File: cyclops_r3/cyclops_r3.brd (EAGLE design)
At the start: 124.5 x 79.9 mm, 105 parts, among them Q1 BC817, Q2 IRF510, U1 MCP4921, U2 MCP4022-50k, U3 317-N, U4 TLV3701, U5 337-N, U6 ADR03, U7 OP1177, U8 LTC2052HV, U9 ZXTD45

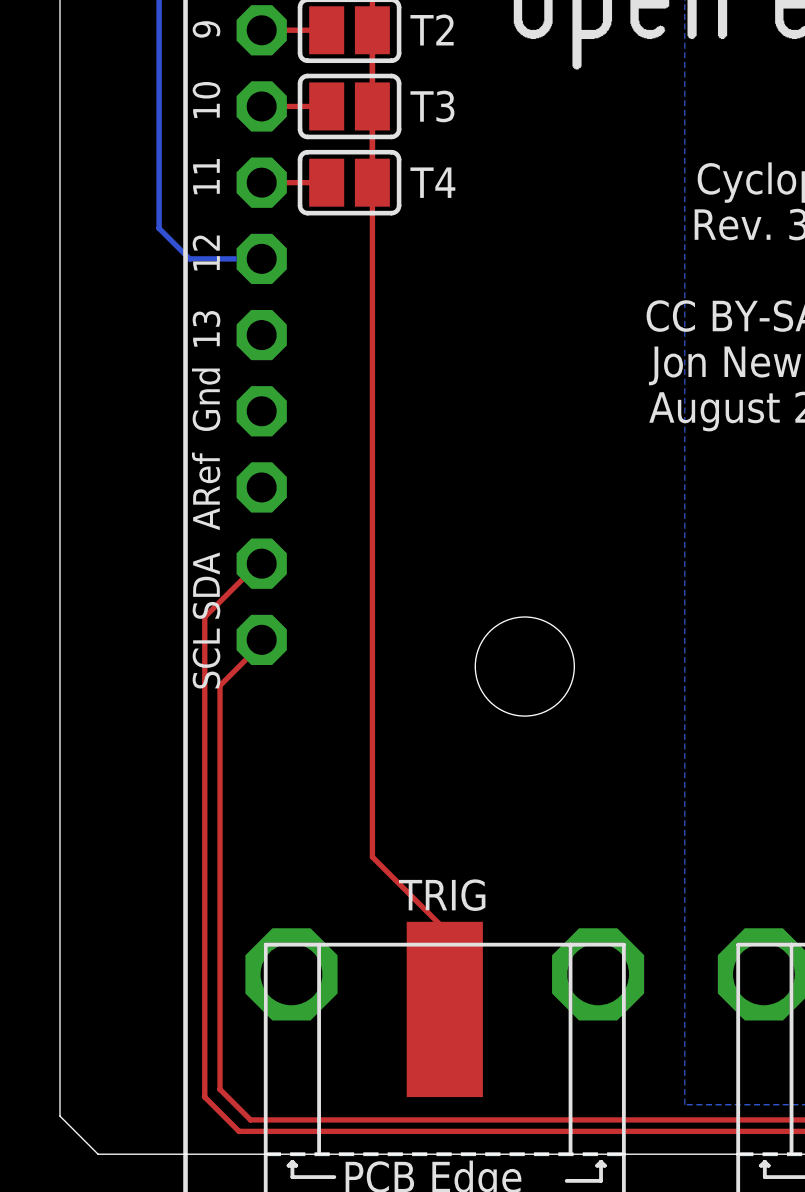
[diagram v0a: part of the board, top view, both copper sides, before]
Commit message: Added pullups to the i2c bus to the PD interface.
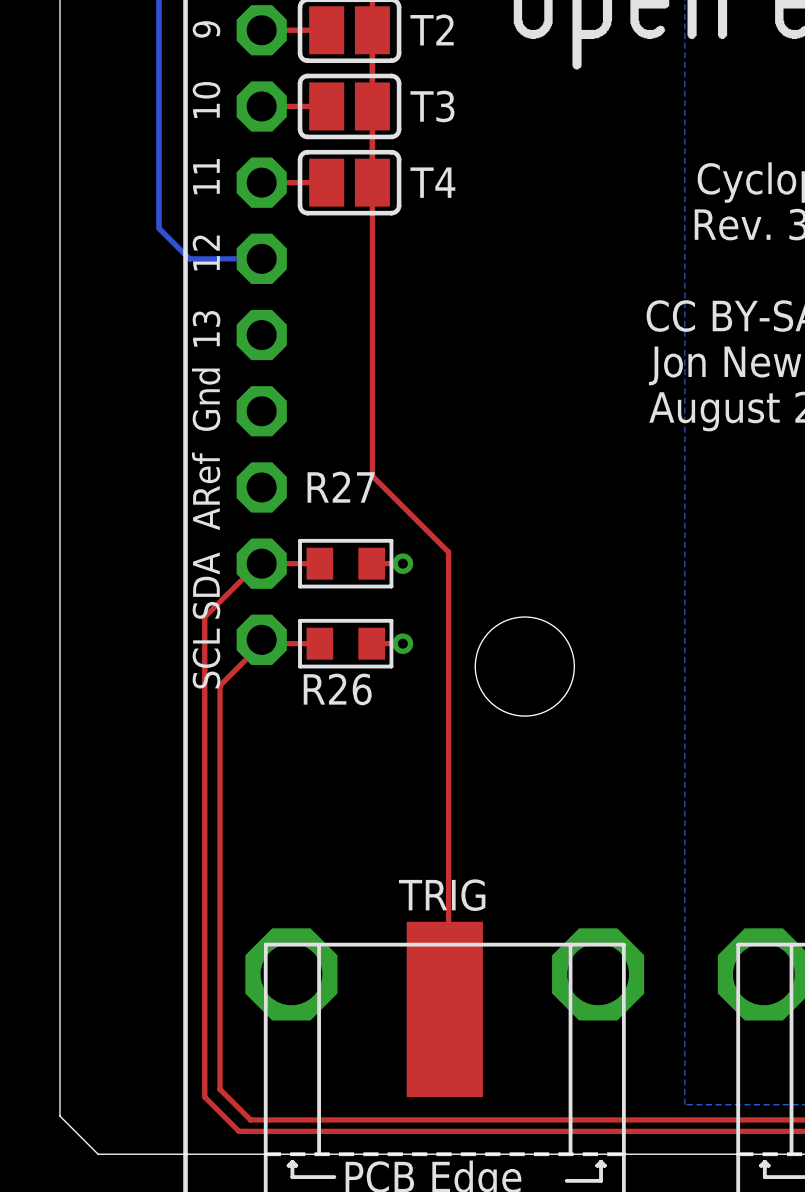
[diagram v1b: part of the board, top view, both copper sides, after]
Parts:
- added R26, R27: 10k, cyclops:0603
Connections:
- net +5V: now also R26.1, R27.1
- net SCL: now also R26.2
- net SDA: now also R27.2
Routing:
- net TRIG: track 41.3 -> 44.0 mm
- net +5V: track 10.9 -> 12.9 mm, vias 3 -> 5
- net SCL: track 96.7 -> 98.7 mm
- net SDA: track 101.8 -> 103.7 mm
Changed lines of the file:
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@@
 <grid distance="0.005" unitdist="inch" unit="inch" style="lines" multiple="1" display="yes" altdistance="0.025" altunitdist="inch" altunit="inch"/>
 <layers>
-<layer number="1" name="Top" color="4" fill="1" visible="no" active="yes"/>
+<layer number="1" name="Top" color="4" fill="1" visible="yes" active="yes"/>
 <layer number="2" name="Route2" color="1" fill="3" visible="no" active="yes"/>
 <layer number="3" name="Route3" color="4" fill="3" visible="no" active="no"/>
@@
 <attribute name="VALUE" x="61.214" y="56.388" size="1.016" layer="27" font="vector" ratio="18" align="center-left"/>
 </element>
+<element name="R26" library="cyclops" package="0603" value="10k" x="9.525" y="18.669" smashed="yes" rot="R180">
+<attribute name="MN" value="Panasonic" x="9.525" y="18.669" size="1.778" layer="27" rot="R180" display="off"/>
+<attribute name="DK" value="PxxxxHTR-ND" x="9.525" y="18.669" size="1.778" layer="27" rot="R180" display="off"/>
+<attribute name="MPN" value="ERJ-3EKFxxxxV" x="9.525" y="18.669" size="1.778" layer="27" rot="R180" display="off"/>
+<attribute name="NAME" x="8.001" y="17.145" size="1.016" layer="25" font="vector" ratio="18" rot="R180" align="center-right"/>
+<attribute name="VALUE" x="8.001" y="16.002" size="1.016" layer="27" font="vector" ratio="18" align="center-left"/>
+</element>
+<element name="R27" library="cyclops" package="0603" value="10k" x="9.525" y="21.336" smashed="yes" rot="R180">
+<attribute name="MN" value="Panasonic" x="9.525" y="21.336" size="1.778" layer="27" rot="R180" display="off"/>
+<attribute name="DK" value="PxxxxHTR-ND" x="9.525" y="21.336" size="1.778" layer="27" rot="R180" display="off"/>
+<attribute name="MPN" value="ERJ-3EKFxxxxV" x="9.525" y="21.336" size="1.778" layer="27" rot="R180" display="off"/>
+<attribute name="NAME" x="8.128" y="23.876" size="1.016" layer="25" font="vector" ratio="18" rot="R180" align="center-right"/>
+<attribute name="VALUE" x="8.128" y="22.733" size="1.016" layer="27" font="vector" ratio="18" align="center-left"/>
+</element>
 </elements>
 <signals>
@@
 <wire x1="29.972" y1="57.912" x2="29.4386" y2="58.4454" width="0.4064" layer="1"/>
 <wire x1="29.33" y1="58.4454" x2="29.4386" y2="58.4454" width="0.4064" layer="1"/>
+<contactref element="R27" pad="1"/>
+<contactref element="R26" pad="1"/>
+<via x="11.43" y="18.669" extent="1-16" drill="0.3302"/>
+<via x="11.43" y="21.336" extent="1-16" drill="0.3302"/>
+<wire x1="10.3886" y1="21.336" x2="11.43" y2="21.336" width="0.1778" layer="1"/>
+<wire x1="10.3886" y1="18.669" x2="11.43" y2="18.669" width="0.1778" layer="1"/>
 </signal>
 <signal name="SCLK">
@@
 <contactref element="TRIG" pad="1"/>
 <wire x1="12.827" y1="6.477" x2="12.827" y2="9.144" width="0.1778" layer="1"/>
-<wire x1="12.827" y1="9.144" x2="10.414" y2="11.557" width="0.1778" layer="1"/>
-<wire x1="10.414" y1="11.557" x2="10.414" y2="34.036" width="0.1778" layer="1"/>
 <wire x1="10.414" y1="34.036" x2="10.414" y2="39.116" width="0.1778" layer="1"/>
 <wire x1="10.414" y1="39.116" x2="10.414" y2="36.576" width="0.1778" layer="1"/>
 <wire x1="10.414" y1="36.576" x2="10.414" y2="34.036" width="0.1778" layer="1"/>
 <wire x1="10.414" y1="39.116" x2="10.414" y2="41.656" width="0.1778" layer="1"/>
+<wire x1="10.414" y1="34.036" x2="10.414" y2="24.257" width="0.1778" layer="1"/>
+<wire x1="10.414" y1="24.257" x2="12.954" y2="21.717" width="0.1778" layer="1"/>
+<wire x1="12.954" y1="21.717" x2="12.954" y2="6.604" width="0.1778" layer="1"/>
+<wire x1="12.954" y1="6.604" x2="12.827" y2="6.477" width="0.1778" layer="1"/>
 </signal>
 <signal name="T0">
@@
 <wire x1="76.708" y1="0.508" x2="80.899" y2="4.699" width="0.1778" layer="1"/>
 <wire x1="80.899" y1="4.699" x2="80.899" y2="8.763" width="0.1778" layer="1"/>
+<contactref element="R27" pad="2"/>
+<wire x1="8.6614" y1="21.336" x2="6.724" y2="21.336" width="0.1778" layer="1"/>
 </signal>
 <signal name="SCL">
@@
 <wire x1="76.5302" y1="0.8382" x2="78.359" y2="2.667" width="0.1778" layer="1"/>
 <wire x1="78.359" y1="2.667" x2="78.359" y2="8.763" width="0.1778" layer="1"/>
+<contactref element="R26" pad="2"/>
+<wire x1="8.6614" y1="18.669" x2="6.724" y2="18.669" width="0.1778" layer="1"/>
+<wire x1="6.724" y1="18.669" x2="6.724" y2="18.796" width="0.1778" layer="1"/>
 </signal>
 <signal name="N$11">

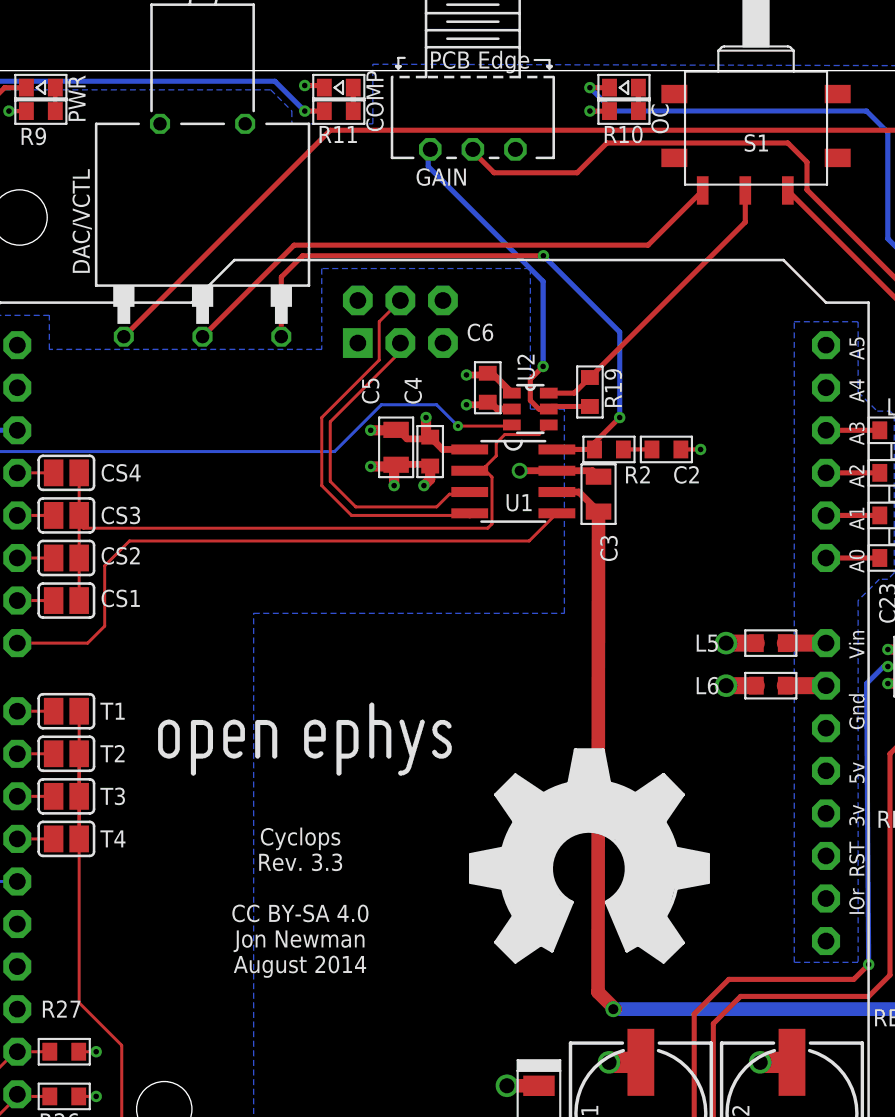
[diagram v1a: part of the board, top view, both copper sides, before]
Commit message: The hole size for the solder lugs on the DAC/VCTL switch were too small. This has been fixed.
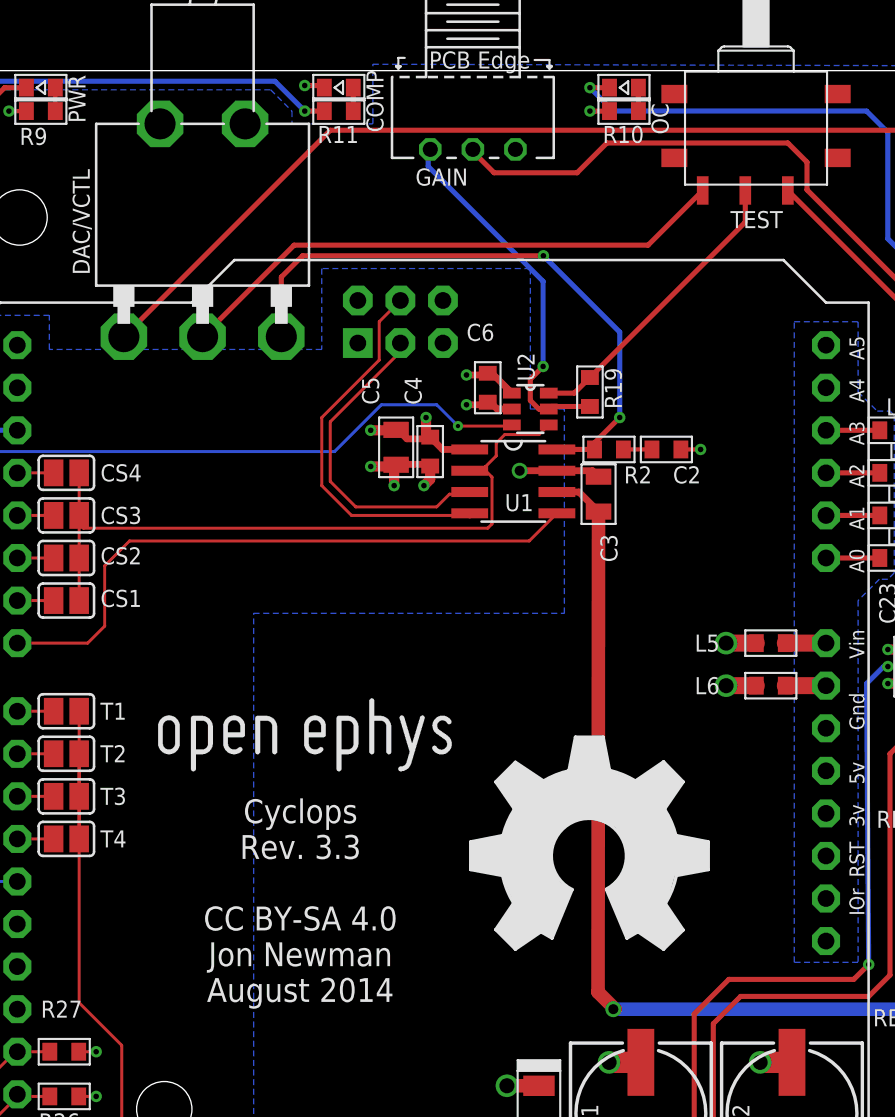
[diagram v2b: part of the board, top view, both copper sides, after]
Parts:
- DAC/VCTL: value JS102 -> 2M1
- TEST: value TEST -> CFPA
- moved U$31 0.76 mm to (33.8, 27.4)
- moved U$30 0.25 mm to (14.5, 37.6)
- renumbered S1 to TEST
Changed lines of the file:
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@@
 <layer number="28" name="bValues" color="7" fill="1" visible="yes" active="yes"/>
 <layer number="29" name="tStop" color="7" fill="3" visible="no" active="yes"/>
-<layer number="30" name="bStop" color="7" fill="6" visible="yes" active="yes"/>
+<layer number="30" name="bStop" color="7" fill="6" visible="no" active="yes"/>
 <layer number="31" name="tCream" color="7" fill="4" visible="no" active="yes"/>
 <layer number="32" name="bCream" color="7" fill="5" visible="no" active="yes"/>
@@
 <vertex x="108.839" y="45.974"/>
 </polygon>
-<text x="23.622" y="30.353" size="1.016" layer="21" font="vector" ratio="18" align="center">Cyclops
+<text x="23.622" y="30.353" size="1.4224" layer="21" font="vector" ratio="18" align="center">Cyclops
 Rev. 3.3
 CC BY-SA 4.0
@@
 <attribute name="VALUE" x="42.665" y="15.748" size="1.016" layer="27" font="vector" ratio="18" rot="R90"/>
 </element>
-<element name="S1" library="cyclops" package="CFPA" value="TEST" x="50.807" y="76.581" smashed="yes" rot="R270">
-<attribute name="NAME" x="50.045" y="75.057" size="1.016" layer="25" font="vector" ratio="18"/>
-<attribute name="VALUE" x="49.029" y="70.231" size="1.016" layer="27" font="vector" ratio="18"/>
+<element name="TEST" library="cyclops" package="CFPA" value="CFPA" x="50.807" y="76.581" smashed="yes" rot="R270">
+<attribute name="NAME" x="49.283" y="70.485" size="1.016" layer="25" font="vector" ratio="18"/>
+<attribute name="VALUE" x="49.029" y="77.978" size="1.016" layer="27" font="vector" ratio="18"/>
 </element>
 <element name="U9" library="cyclops" package="SOT23-6" value="ZXTD45" x="87.63" y="45.332" smashed="yes" rot="R270">
@@
 <attribute name="VALUE" x="35.306" y="73.025" size="1.016" layer="27" font="vector" ratio="18"/>
 </element>
-<element name="DAC/VCTL" library="cyclops" package="2M1-SP1-T2-B4-M6RE" value="JS102" x="17.78" y="76.2" smashed="yes" rot="R270">
+<element name="DAC/VCTL" library="cyclops" package="2M1-SP1-T2-B4-M6RE" value="2M1" x="17.78" y="76.2" smashed="yes" rot="R270">
 <attribute name="NAME" x="11.049" y="67.691" size="1.016" layer="25" font="vector" ratio="18" rot="R90"/>
-<attribute name="VALUE" x="15.621" y="73.914" size="1.016" layer="27" font="vector" ratio="18"/>
+<attribute name="VALUE" x="16.383" y="73.914" size="1.016" layer="27" font="vector" ratio="18"/>
 </element>
 <element name="L6" library="cyclops" package="0603" value="MPZ1608" x="51.689" y="43.18" smashed="yes" rot="R180">
@@
 <attribute name="VALUE" x="67.691" y="38.1" size="1.016" layer="27" font="vector" ratio="18" align="center-left"/>
 </element>
-<element name="U$30" library="open-ephys" package="OPEN_EPHYS_LOGO" value="OPEN_EPHYS_LOGO" x="14.478" y="37.338" smashed="yes"/>
-<element name="U$31" library="ohw-logo" package="OSHW_FILLX500_NOTEXT" value="" x="33.782" y="26.67" smashed="yes"/>
+<element name="U$30" library="open-ephys" package="OPEN_EPHYS_LOGO" value="OPEN_EPHYS_LOGO" x="14.478" y="37.592" smashed="yes"/>
+<element name="U$31" library="ohw-logo" package="OSHW_FILLX500_NOTEXT" value="" x="33.782" y="27.432" smashed="yes"/>
 <element name="HEATSINK" library="cyclops" package="BDN18" value="BDN18" x="108.966" y="22.225" smashed="yes" rot="MR0">
 <attribute name="NAME" x="108.966" y="69.977" size="1.016" layer="26" font="vector" ratio="18" rot="MR0"/>
@@
 </signal>
 <signal name="VCTL">
-<contactref element="S1" pad="2"/>
+<contactref element="TEST" pad="2"/>
 <contactref element="R19" pad="2"/>
 <wire x1="50.167" y1="73.277" x2="50.167" y2="72.731" width="0.3048" layer="1"/>
@@
 </signal>
 <signal name="N$34">
-<contactref element="S1" pad="3"/>
+<contactref element="TEST" pad="3"/>
 <contactref element="DAC/VCTL" pad="2"/>
 <wire x1="17.78" y1="64.008" x2="23.241" y2="69.469" width="0.3048" layer="1"/>
@@
 </signal>
 <signal name="REF5.0">
-<contactref element="S1" pad="1"/>
+<contactref element="TEST" pad="1"/>
 <contactref element="R17" pad="2"/>
 <contactref element="C20" pad="1"/>
